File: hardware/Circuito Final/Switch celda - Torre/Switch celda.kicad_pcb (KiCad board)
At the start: 2 copper layers, 98.6 x 38 mm, 32 parts, among them Q1 MMBT2222A, Q2 MMBT2907A, Q3 MMBT2222A

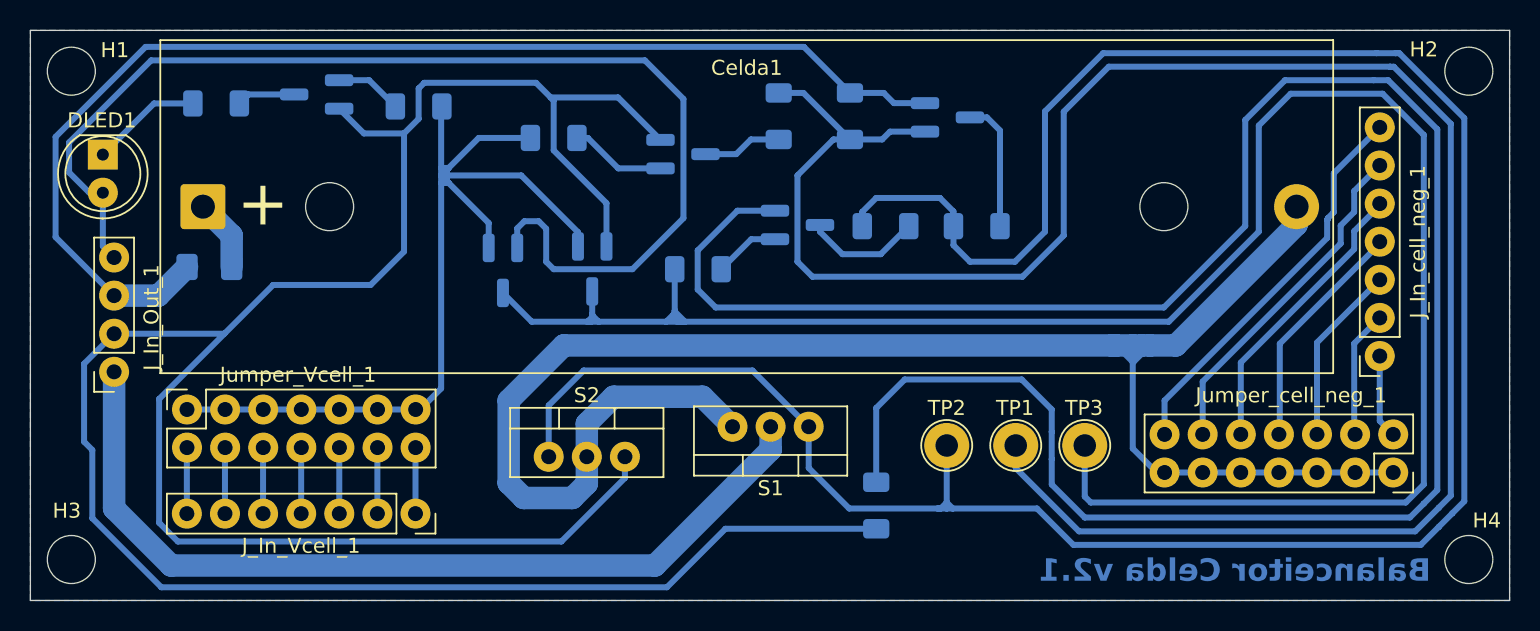
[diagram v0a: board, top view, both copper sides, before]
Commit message: update de valores del codigo y subida de archivos historicos de los PCBs
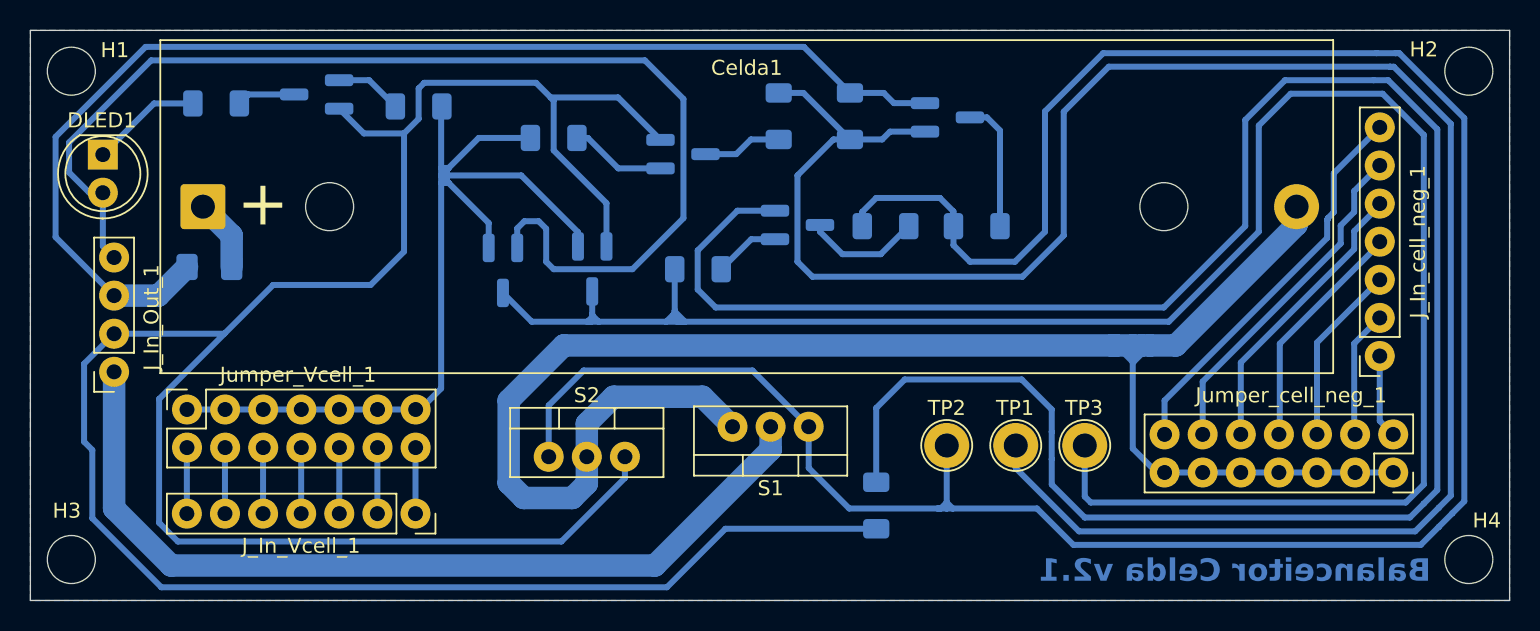
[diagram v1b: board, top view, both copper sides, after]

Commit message: update PCB celda con los modelos 3D corregidos
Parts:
- Jumper_Vcell_1, Jumper_cell_neg_1: footprint Connector_PinSocket_2.54mm:PinSocket_2x07_P2.54mm_Vertical -> Connector_PinHeader_2.54mm:PinHeader_2x07_P2.54mm_Vertical
- moved Jumper_Vcell_1 15.2 mm to (125.8, 109.6), turned to -90 degrees
- moved Jumper_cell_neg_1 15.2 mm to (175.7, 113.8), turned to 90 degrees
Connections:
- Jumper_Vcell_1 pad 10: Vcell3 -> Vcell5
- Jumper_Vcell_1 pad 12: Vcell2 -> Vcell6
- Jumper_Vcell_1 pad 14: Vcell1 -> Vcell7
- Jumper_Vcell_1 pad 2: Vcell7 -> Vcell1
- Jumper_Vcell_1 pad 4: Vcell6 -> Vcell2
- Jumper_Vcell_1 pad 6: Vcell5 -> Vcell3
- Jumper_cell_neg_1 pad 10: cell_neg5 -> cell_neg3
- Jumper_cell_neg_1 pad 12: cell_neg6 -> cell_neg2
- Jumper_cell_neg_1 pad 14: cell_neg7 -> cell_neg1
- Jumper_cell_neg_1 pad 2: cell_neg1 -> cell_neg7
- Jumper_cell_neg_1 pad 4: cell_neg2 -> cell_neg6
- Jumper_cell_neg_1 pad 6: cell_neg3 -> cell_neg5
